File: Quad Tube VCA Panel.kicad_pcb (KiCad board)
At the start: 2 copper layers, 162.6 x 128.5 mm, 0 parts

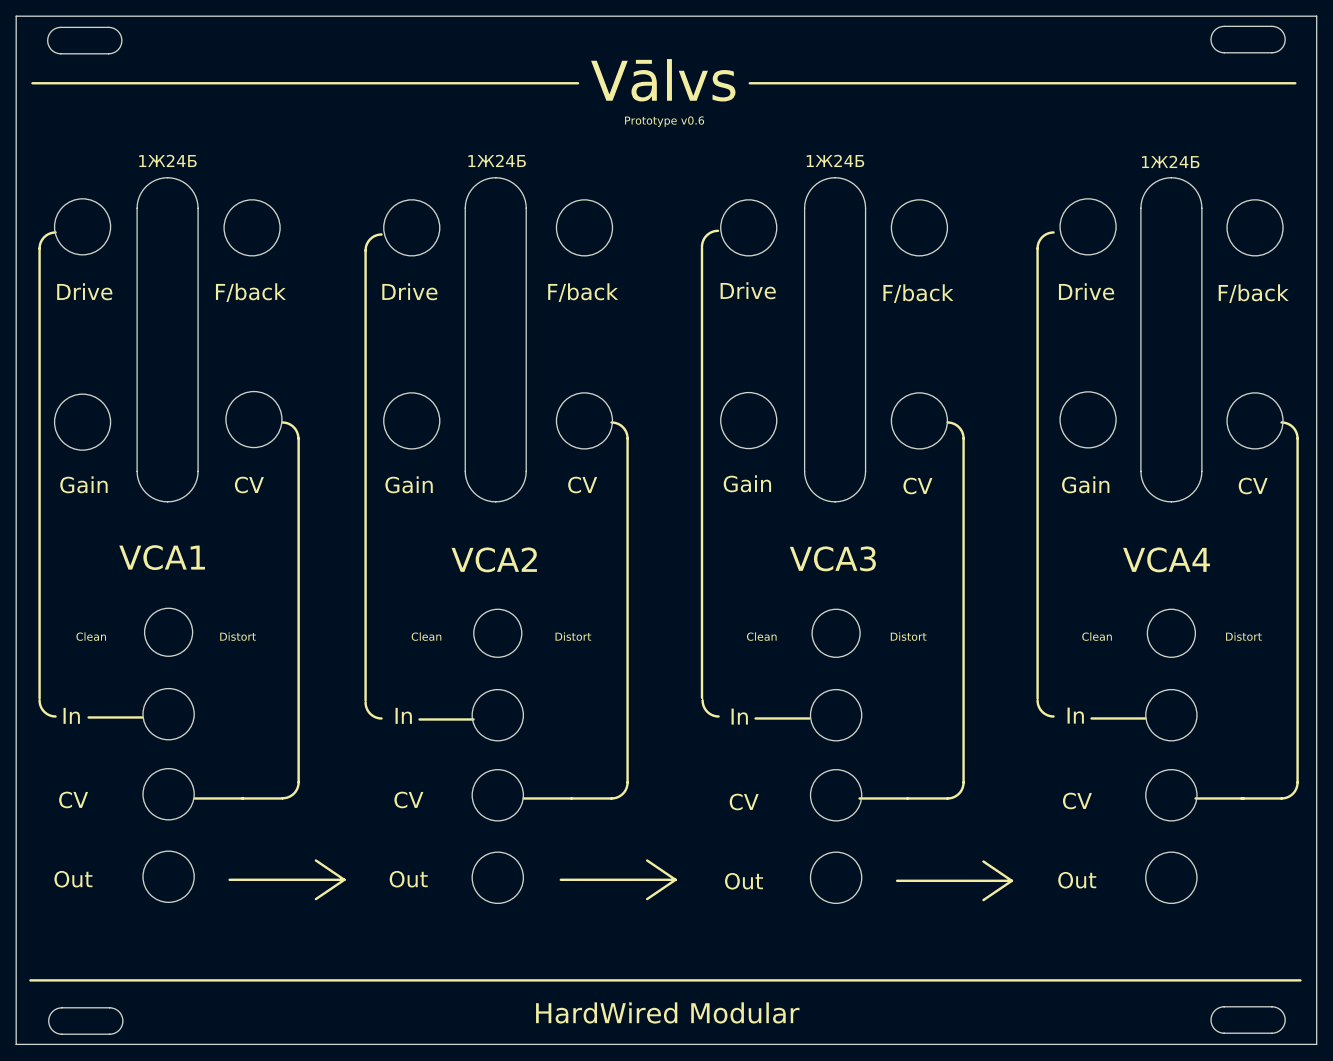
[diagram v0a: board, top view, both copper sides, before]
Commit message: adds copper to panel
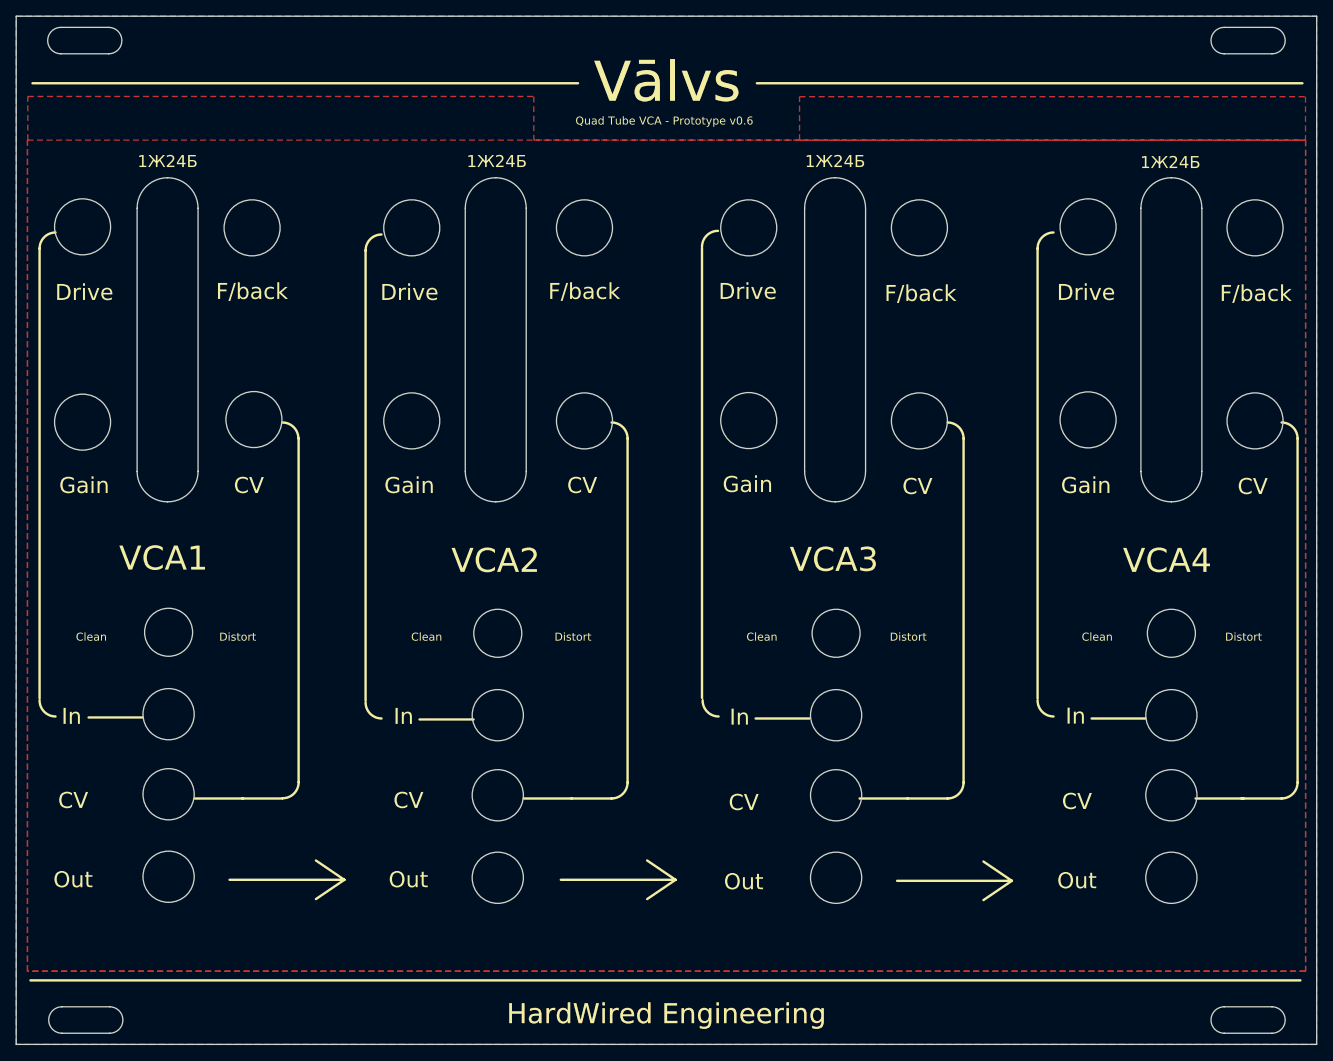
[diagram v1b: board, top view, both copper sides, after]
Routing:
- added copper zone on B.Cu, net (none)
- added copper zone on F.Cu, net (none)
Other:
- outline, holes or cut-outs redrawn
- board text added: "HardWired Engineering"
- board text added: "Quad Tube VCA - Prototype v0.6"
- board text removed: "HardWired Modular"
- board text removed: "Prototype v0.6"
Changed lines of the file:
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@@
   (general
     (thickness 1.6)
-    (drawings 175)
+    (drawings 177)
     (tracks 0)
     (zones 0)
@@
     (uvia_drill 0.1)
   )
+  (gr_text Vālvs (at 88.138 68.961) (layer F.Cu)
+    (effects (font (size 5 5) (thickness 0.5)))
+  )
+  (gr_text "HardWired Engineering" (at 88.011 185.42) (layer F.Cu)
+    (effects (font (size 2.5 2.5) (thickness 0.25)))
+  )
   (gr_line (start 134.403 146.241) (end 134.403 145.991) (layer F.SilkS) (width 0.12))
   (gr_line (start 141.153 148.491) (end 147.903 148.491) (layer F.SilkS) (width 0.3))
@@
   (gr_line (start 8.509 181.229) (end 167.259 181.229) (layer F.SilkS) (width 0.3))
   (gr_line (start 8.763 69.088) (end 76.962 69.088) (layer F.SilkS) (width 0.3))
-  (gr_line (start 98.425 69.088) (end 166.624 69.088) (layer F.SilkS) (width 0.3))
+  (gr_line (start 99.314 69.088) (end 167.513 69.088) (layer F.SilkS) (width 0.3))
   (gr_text 1Ж24Б (at 151.003 78.994) (layer F.SilkS)
     (effects (font (size 1.5 1.5) (thickness 0.2)))
@@
   (gr_line (start 47.752 168.656) (end 44.196 166.243) (layer F.SilkS) (width 0.3))
   (gr_line (start 33.401 168.656) (end 47.752 168.656) (layer F.SilkS) (width 0.3))
-  (gr_text "HardWired Modular" (at 88.011 185.42) (layer F.SilkS)
+  (gr_text "HardWired Engineering" (at 88.011 185.42) (layer F.SilkS)
     (effects (font (size 2.5 2.5) (thickness 0.25)))
   )
@@
     (effects (font (size 2 2) (thickness 0.2)))
   )
-  (gr_text "Prototype v0.6" (at 87.757 73.787) (layer F.SilkS)
-    (effects (font (size 1 1) (thickness 0.15)))
-  )
-  (gr_text F/back (at 161.29 95.377) (layer F.SilkS)
+  (gr_text "Quad Tube VCA - Prototype v0.6" (at 87.757 73.787) (layer F.SilkS)
+    (effects (font (size 1 1) (thickness 0.15)))
+  )
+  (gr_text F/back (at 161.671 95.377) (layer F.SilkS)
     (effects (font (size 2 2) (thickness 0.2)))
   )
@@
     (effects (font (size 2 2) (thickness 0.2)))
   )
-  (gr_text F/back (at 119.38 95.377) (layer F.SilkS)
+  (gr_text F/back (at 119.761 95.377) (layer F.SilkS)
     (effects (font (size 2 2) (thickness 0.2)))
   )
@@
     (effects (font (size 2 2) (thickness 0.2)))
   )
-  (gr_text F/back (at 77.47 95.25) (layer F.SilkS)
+  (gr_text F/back (at 77.724 95.123) (layer F.SilkS)
     (effects (font (size 2 2) (thickness 0.2)))
   )
@@
     (effects (font (size 2 2) (thickness 0.2)))
   )
-  (gr_text F/back (at 35.941 95.25) (layer F.SilkS)
+  (gr_text F/back (at 36.195 95.123) (layer F.SilkS)
     (effects (font (size 2 2) (thickness 0.2)))
   )
@@
     (effects (font (size 2 2) (thickness 0.2)))
   )
-  (gr_text Vālvs (at 87.757 68.961) (layer F.SilkS)
+  (gr_text Vālvs (at 88.138 68.961) (layer F.SilkS)
     (effects (font (size 5 5) (thickness 0.5)))
   )
@@
   (gr_line (start 157.734 184.531) (end 163.703 184.531) (layer Edge.Cuts) (width 0.05))
   (gr_arc (start 163.703 186.182) (end 163.703 187.833) (angle -180) (layer Edge.Cuts) (width 0.05))
-  (gr_line (start 18.415 187.96) (end 12.446 187.96) (layer Edge.Cuts) (width 0.05))
-  (gr_arc (start 18.415 186.309) (end 18.415 187.96) (angle -180) (layer Edge.Cuts) (width 0.05))
-  (gr_line (start 12.446 184.658) (end 18.415 184.658) (layer Edge.Cuts) (width 0.05))
-  (gr_arc (start 12.446 186.309) (end 12.446 184.658) (angle -180) (layer Edge.Cuts) (width 0.05))
-  (gr_line (start 163.703 65.278) (end 157.734 65.278) (layer Edge.Cuts) (width 0.05))
-  (gr_arc (start 163.703 63.627) (end 163.703 65.278) (angle -180) (layer Edge.Cuts) (width 0.05))
-  (gr_line (start 157.734 61.976) (end 163.703 61.976) (layer Edge.Cuts) (width 0.05))
-  (gr_arc (start 157.734 63.627) (end 157.734 61.976) (angle -180) (layer Edge.Cuts) (width 0.05))
+  (gr_line (start 18.415 187.833) (end 12.446 187.833) (layer Edge.Cuts) (width 0.05))
+  (gr_arc (start 18.415 186.182) (end 18.415 187.833) (angle -180) (layer Edge.Cuts) (width 0.05))
+  (gr_line (start 12.446 184.531) (end 18.415 184.531) (layer Edge.Cuts) (width 0.05))
+  (gr_arc (start 12.446 186.182) (end 12.446 184.531) (angle -180) (layer Edge.Cuts) (width 0.05))
+  (gr_line (start 163.703 65.405) (end 157.734 65.405) (layer Edge.Cuts) (width 0.05))
+  (gr_arc (start 163.703 63.754) (end 163.703 65.405) (angle -180) (layer Edge.Cuts) (width 0.05))
+  (gr_line (start 157.734 62.103) (end 163.703 62.103) (layer Edge.Cuts) (width 0.05))
+  (gr_arc (start 157.734 63.754) (end 157.734 62.103) (angle -180) (layer Edge.Cuts) (width 0.05))
   (gr_line (start 12.319 62.103) (end 18.288 62.103) (layer Edge.Cuts) (width 0.05))
   (gr_line (start 18.288 65.405) (end 12.319 65.405) (layer Edge.Cuts) (width 0.05))
@@
   (gr_circle (center 15.028 87.035) (end 18.528 87.035) (layer Edge.Cuts) (width 0.05))
   (gr_line (start 169.291 189.23) (end 169.291 60.706) (layer Edge.Cuts) (width 0.05))
+  (zone (net 0) (net_name "") (layer B.Cu) (hatch edge 0.508)
+    (connect_pads (clearance 0.508))
+    (min_thickness 0.254)
+    (fill yes (arc_segments 32) (thermal_gap 0.508) (thermal_bridge_width 0.508))
+    (polygon
+      (pts
+        (xy 169.291 189.23) (xy 6.731 189.23) (xy 6.731 60.706) (xy 169.291 60.706)
+      )
+    )
+  )
+  (zone (net 0) (net_name "") (layer F.Cu) (hatch edge 0.508)
+    (connect_pads (clearance 0.508))
+    (min_thickness 0.254)
+    (fill yes (arc_segments 32) (thermal_gap 0.508) (thermal_bridge_width 0.508))
+    (polygon
+      (pts
+        (xy 167.894 76.227411) (xy 104.648 76.227411) (xy 104.648 70.766411) (xy 167.894 70.766411)
+      )
+    )
+  )
+  (zone (net 0) (net_name "") (layer F.Cu) (hatch edge 0.508)
+    (connect_pads (clearance 0.508))
+    (min_thickness 0.254)
+    (fill yes (arc_segments 32) (thermal_gap 0.508) (thermal_bridge_width 0.508))
+    (polygon
+      (pts
+        (xy 71.432246 76.2) (xy 167.913053 76.2) (xy 167.913053 180.086) (xy 8.147053 180.086) (xy 8.147053 76.2)
+        (xy 8.186246 76.2) (xy 8.186246 70.739) (xy 71.432246 70.739)
+      )
+    )
+  )
+  (zone (net 0) (net_name "") (layer F.Cu) (hatch edge 0.508)
+    (connect_pads (clearance 0.508))
+    (min_thickness 0.254)
+    (fill yes (arc_segments 32) (thermal_gap 0.508) (thermal_bridge_width 0.508))
+    (polygon
+      (pts
+        (xy 167.894 180.086) (xy 8.128 180.086) (xy 8.128 76.2) (xy 167.894 76.2)
+      )
+    )
+  )
 )

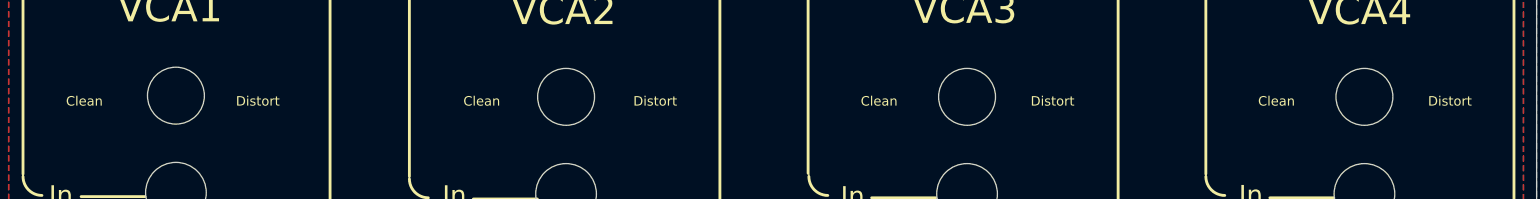
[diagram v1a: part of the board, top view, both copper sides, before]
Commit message: text positions
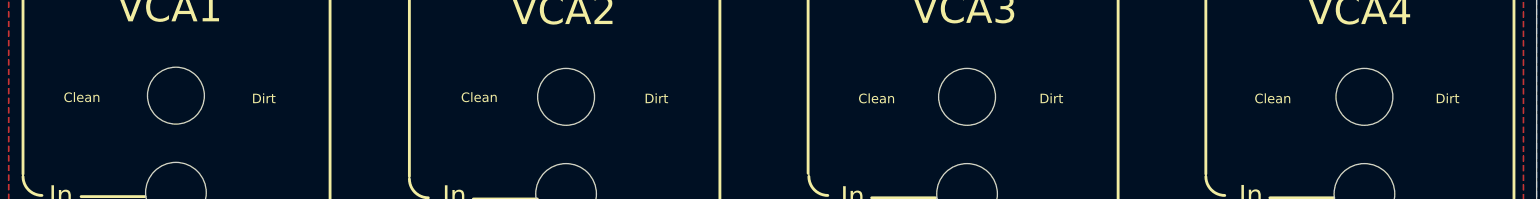
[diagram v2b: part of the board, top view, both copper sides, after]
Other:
- board text added: "Dirt"
- board text removed: "Distort"
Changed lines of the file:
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@@
     (effects (font (size 3 3) (thickness 0.3)))
   )
-  (gr_text "Distort\n" (at 160.147 138.303) (layer F.SilkS)
+  (gr_text Dirt (at 159.893 138.049) (layer F.SilkS)
     (effects (font (size 1 1) (thickness 0.15)))
   )
-  (gr_text Clean (at 141.859 138.303) (layer F.SilkS)
+  (gr_text Clean (at 141.478 138.049) (layer F.SilkS)
     (effects (font (size 1 1) (thickness 0.15)))
   )
-  (gr_text "Distort\n" (at 118.237 138.303) (layer F.SilkS)
+  (gr_text Dirt (at 118.11 138.049) (layer F.SilkS)
     (effects (font (size 1 1) (thickness 0.15)))
   )
-  (gr_text Clean (at 99.949 138.303) (layer F.SilkS)
+  (gr_text Clean (at 99.695 138.049) (layer F.SilkS)
     (effects (font (size 1 1) (thickness 0.15)))
   )
-  (gr_text "Distort\n" (at 76.327 138.303) (layer F.SilkS)
+  (gr_text Dirt (at 76.454 138.049) (layer F.SilkS)
     (effects (font (size 1 1) (thickness 0.15)))
   )
-  (gr_text Clean (at 58.039 138.303) (layer F.SilkS)
+  (gr_text Clean (at 57.785 137.922) (layer F.SilkS)
     (effects (font (size 1 1) (thickness 0.15)))
   )
-  (gr_text "Distort\n" (at 34.417 138.303) (layer F.SilkS)
+  (gr_text Dirt (at 35.052 138.049) (layer F.SilkS)
     (effects (font (size 1 1) (thickness 0.15)))
   )
-  (gr_text Clean (at 16.129 138.303) (layer F.SilkS)
+  (gr_text Clean (at 15.875 137.922) (layer F.SilkS)
     (effects (font (size 1 1) (thickness 0.15)))
   )
